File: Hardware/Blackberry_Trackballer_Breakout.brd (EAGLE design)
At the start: 59.7 x 24.1 mm, 41 parts, among them U1 HALL-EFFECTSMD, U2 HALL-EFFECTSMD, U3 HALL-EFFECTSMD, U4 HALL-EFFECTSMD

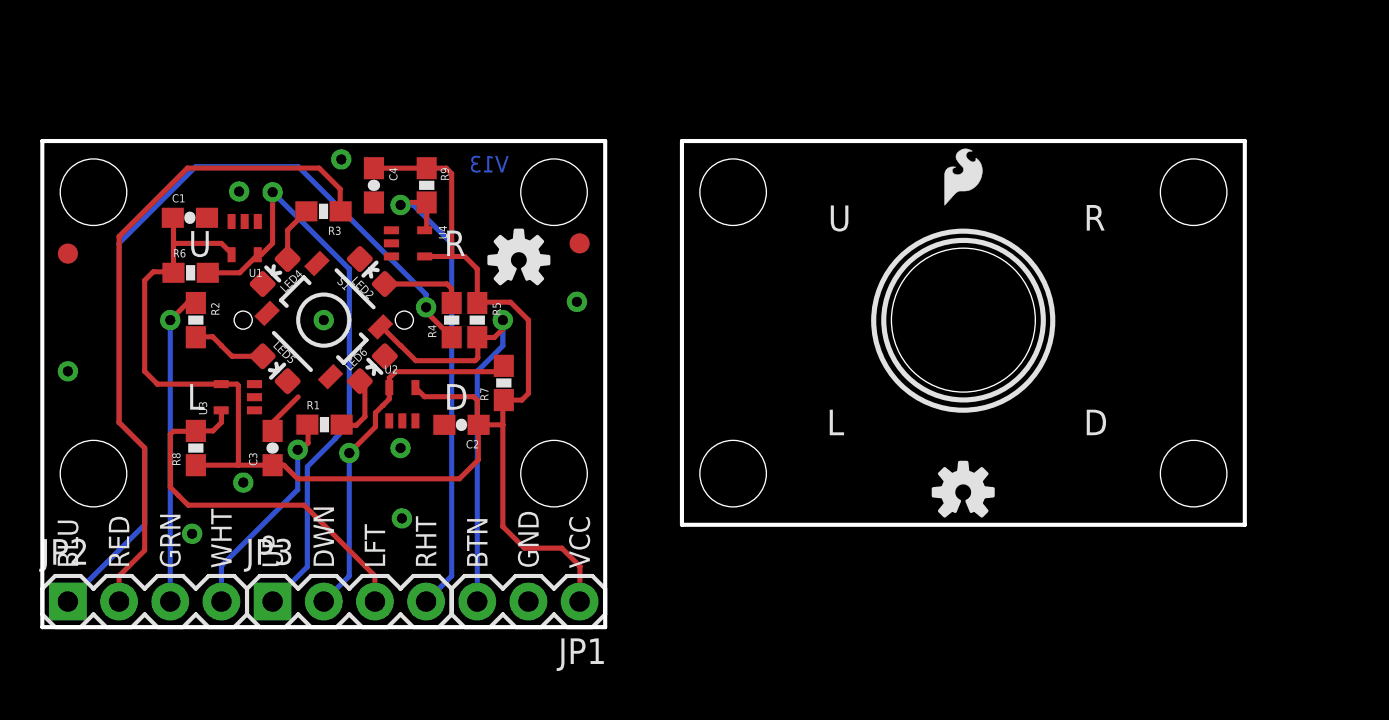
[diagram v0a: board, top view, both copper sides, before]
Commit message: initial qc checklist changes.
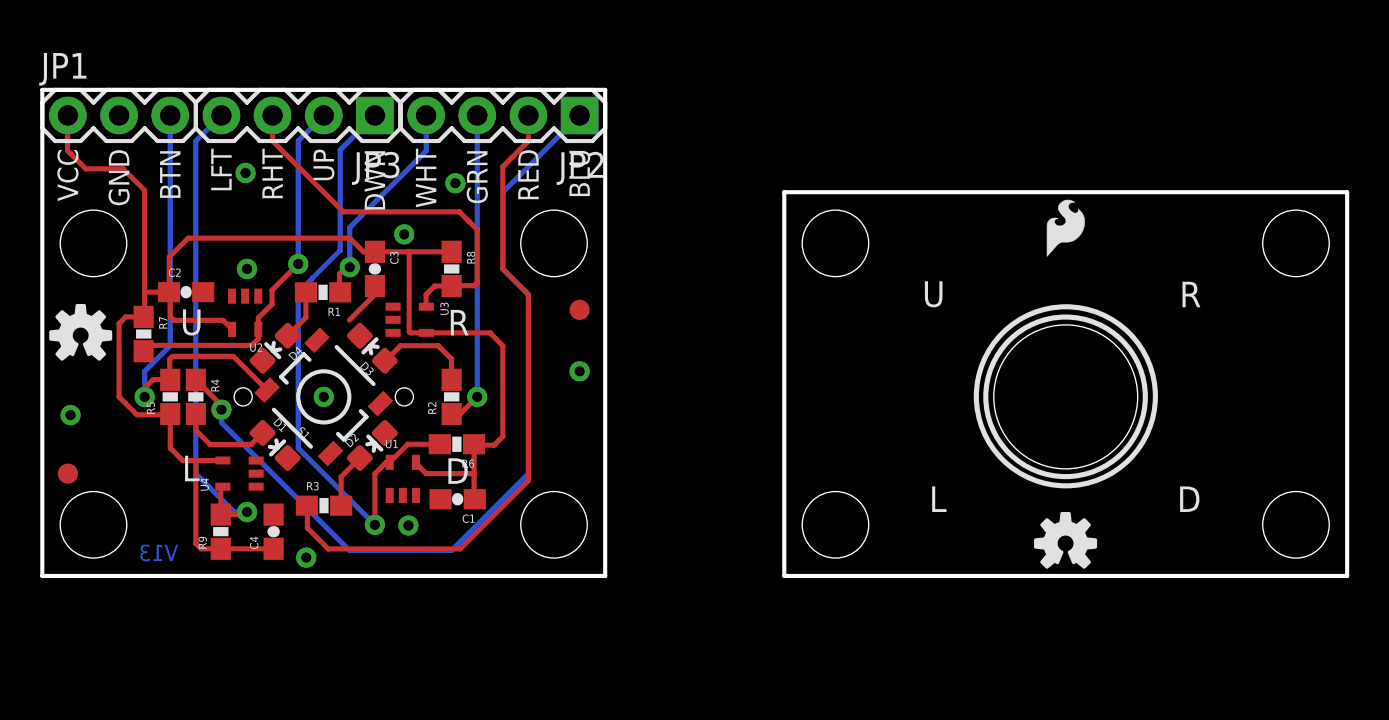
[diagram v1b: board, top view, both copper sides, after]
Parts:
- removed LED2: BLU, SparkFun-LED:LED-0603
- removed LED4: RED, SparkFun-LED:LED-0603
- removed LED5: GRN, SparkFun-LED:LED-0603
- removed LED6: WHT, SparkFun-LED:LED-0603
- removed U$5, U$6, U$9: STAND-OFF, SparkFun:STAND-OFF
- added D1: BLU, SparkFun-LED:LED-0603
- added D2: RED, SparkFun-LED:LED-0603
- added D3: GRN, SparkFun-LED:LED-0603
- added D4: WHT, SparkFun-LED:LED-0603
- added LOGO1: SFE_LOGO_NAME_FLAME.2_INCH, SparkFun-Aesthetics:SFE_LOGO_NAME_FLAME_.2
- added LOGO2: OSHW-LOGOS, SparkFun-Aesthetics:OSHW-LOGO-S
- added U$14: STAND-OFF, SparkFun:STAND-OFF
- U$1: value LOGO-SFENEW -> STAND-OFF; device SparkFun:SFE-NEW-WEBLOGO -> SparkFun:STAND-OFF
- U$11: value (none) -> STAND-OFF; device SparkFun-Aesthetics:OSHW-LOGO-S -> SparkFun:STAND-OFF
- U1, U2, U3, U4: device SparkFun:SC70 -> SparkFun-Sensors:SC70
- moved U$4 59.7 mm to (62.2, 16.5)
- moved JP1 35.0 mm to (1.27, 22.9), turned to 0 degrees
- moved JP2 35.0 mm to (26.7, 22.9), turned to 180 degrees
- moved U$8 31.9 mm to (25.4, 16.5)
- moved E$2 27.9 mm to (1.27, 5.08), turned to 180 degrees
- moved E$1 25.6 mm to (26.7, 13.2), turned to 180 degrees
- moved U$11 24.9 mm to (2.54, 2.54)
- moved JP3 24.7 mm to (16.5, 22.9), turned to 180 degrees
- moved U$1 22.3 mm to (2.54, 16.5), flipped to the top
- moved U$3 21.6 mm to (39.4, 2.54)
- moved R9 20.0 mm to (8.86, 2.20), turned to 90 degrees
- moved C1 19.3 mm to (20.6, 3.81), turned to 180 degrees
- moved R7 18.0 mm to (5.03, 12.0), turned to 270 degrees
- moved C4 17.9 mm to (11.5, 2.20), turned to 90 degrees
- moved R6 15.7 mm to (20.6, 6.54), turned to 180 degrees
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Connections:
- net GND: now also D1.C, D2.C, D3.C, D4.C; no longer LED2.C, LED4.C, LED5.C, LED6.C
- net N$1: now also D3.A; no longer LED5.A
- net N$2: now also D2.A; no longer LED4.A
- net N$3: now also D1.A; no longer LED2.A
- net N$4: now also D4.A; no longer LED6.A
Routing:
- net N$1: track 3.73 -> 4.96 mm
- net N$4: track 3.21 -> 2.58 mm
- net N$3: track 4.54 -> 5.07 mm
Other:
- board size 59.7 x 24.1 mm -> 64.8 x 24.1 mm

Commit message: Schematic Clean up, added Blackberry device...
and trace re routes.
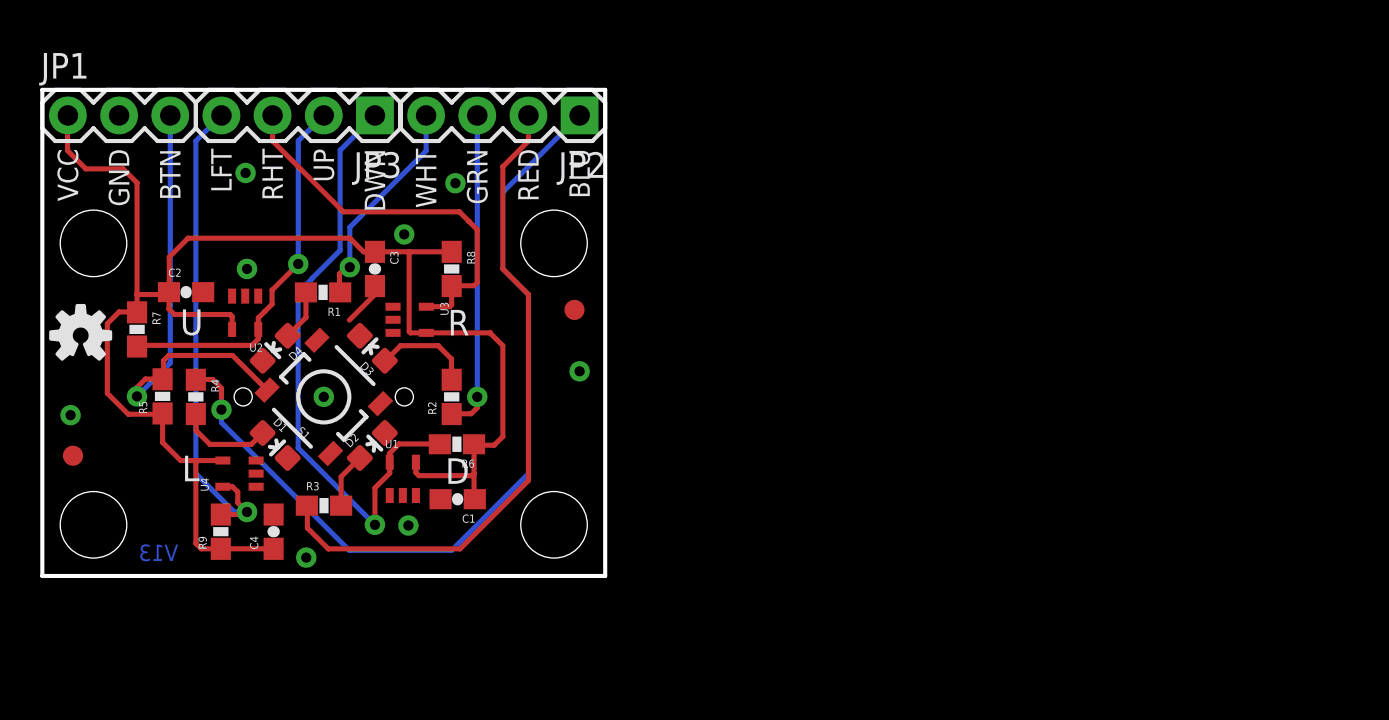
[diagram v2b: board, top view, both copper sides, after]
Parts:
- removed U$10, U$3, U$4, U$7: STAND-OFF, SparkFun:STAND-OFF
- removed U$12: (no value), SparkFun-Aesthetics:OSHW-LOGO-S
- removed U$13: (no value), SparkFun-Aesthetics:SFE-LOGO-FLAME
- moved E$2 0.92 mm to (1.52, 5.97)
- moved R7 0.40 mm to (4.70, 12.2)
- moved R5 0.38 mm to (5.97, 8.92)
- moved E$1 0.25 mm to (26.4, 13.2)
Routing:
- net VCC: track 76.4 -> 77.8 mm
- net RHT: track 24.4 -> 25.0 mm
- net BLU: track 42.0 -> 42.5 mm
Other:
- board size 64.8 x 24.1 mm -> 27.9 x 24.1 mm

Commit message: Added attributes to swch, trackball and whte led
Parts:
- removed U$2: TRACKBALLMECH, SparkFun:TRACKBALL
- added U$3: TRACKBALLMECH, SparkFun-Electromechanical:TRACKBALL
- S1: device SparkFun:TACTILE_SWITCH_SMD-2 -> SparkFun-Electromechanical:TACTILE_SWITCH_SMD-2
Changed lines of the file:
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@@
 <setting verticaltext="up"/>
 </settings>
-<grid distance="0.05" unitdist="inch" unit="inch" style="lines" multiple="1" display="yes" altdistance="0.001" altunitdist="inch" altunit="inch"/>
+<grid distance="0.05" unitdist="inch" unit="inch" style="lines" multiple="1" display="yes" altdistance="0.005" altunitdist="inch" altunit="inch"/>
 <layers>
 <layer number="1" name="Top" color="4" fill="1" visible="yes" active="yes"/>
@@
 <element name="E$1" library="SparkFun" package="FIDUCIAL-1X2" value="FIDUCIAL1X2" x="26.416" y="13.208" rot="R180"/>
 <element name="E$2" library="SparkFun" package="FIDUCIAL-1X2" value="FIDUCIAL1X2" x="1.524" y="5.969" rot="R180"/>
-<element name="S1" library="SparkFun" package="TACTILE_SWITCH_SMD-2" value="SWITCH-MOMENTARY-2SMD-2" x="13.97" y="8.89" rot="R135"/>
+<element name="S1" library="SparkFun-Electromechanical" package="TACTILE_SWITCH_SMD-2" value="SWITCH-MOMENTARY-2SMD-2" x="13.97" y="8.89" rot="R135">
+<attribute name="PROD_ID" value="SWCH-09213" x="13.97" y="8.89" size="1.778" layer="27" rot="R135" display="off"/>
+</element>
 <element name="D1" library="SparkFun-LED" package="LED-0603" value="BLU" x="11.557" y="6.477" rot="R225">
 <attribute name="PROD_ID" value="DIO-08575" x="11.557" y="6.477" size="1.778" layer="27" rot="R225" display="off"/>
@@
 <attribute name="VALUE" value="GREEN" x="16.383" y="11.303" size="1.778" layer="27" rot="R45" display="off"/>
 </element>
-<element name="D4" library="SparkFun-LED" package="LED-0603" value="WHT" x="11.557" y="11.303" rot="R135"/>
+<element name="D4" library="SparkFun-LED" package="LED-0603" value="WHT" x="11.557" y="11.303" rot="R135">
+<attribute name="PROD_ID" value="DIO-09004" x="11.557" y="11.303" size="1.778" layer="27" rot="R135" display="off"/>
+</element>
 <element name="U1" library="SparkFun-Sensors" package="SC70" value="HALL-EFFECTSMD" x="17.895315625" y="4.81965">
 <attribute name="PROD_ID" value="IC-09214" x="17.895315625" y="4.81965" size="1.778" layer="27" display="off"/>
@@
 <element name="JP3" library="SparkFun" package="1X04" value="" x="16.51" y="22.86" rot="R180"/>
 <element name="JP2" library="SparkFun" package="1X04" value="" x="26.67" y="22.86" rot="R180"/>
-<element name="U$2" library="SparkFun" package="TRACKBALL" value="TRACKBALLMECH" x="13.97" y="8.89" rot="R180"/>
 <element name="JP1" library="SparkFun" package="1X03" value="" x="1.27" y="22.86"/>
 <element name="FRAME1" library="SparkFun-Aesthetics" package="CREATIVE_COMMONS" value="FRAME-LETTER" x="-17.252121875" y="-12.7"/>
@@
 <element name="U$11" library="SparkFun" package="STAND-OFF" value="STAND-OFF" x="2.54" y="2.54"/>
 <element name="U$14" library="SparkFun" package="STAND-OFF" value="STAND-OFF" x="25.4" y="2.54"/>
+<element name="U$3" library="SparkFun-Electromechanical" package="TRACKBALL" value="TRACKBALLMECH" x="13.97" y="8.89">
+<attribute name="PROD_ID" value="COMP-09237" x="13.97" y="8.89" size="1.778" layer="27" display="off"/>
+</element>
 </elements>
 <signals>
@@
 </signal>
 </signals>
-<errors>
-</errors>
 </board>
 </drawing>
